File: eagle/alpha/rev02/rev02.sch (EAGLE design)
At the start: 379 parts, among them CN1 HOST, CN2 HOST, IC1 IS45S32160F, IC2 IS45S32160F, IC3 N25Q128A13ES, IC4 N25Q128A13ES, Q1 2N7002, Q3 2N7002, Q5 ASFL1, Q6 2N7002, T1 BC847, T2 BC847, T3 BC818, U1 MC14551BDG, U2 MC74HC1G14DTT1G, U3 ATTINY828R-AU, U4 MC14551BDG, U5 23K640-I/SN, U6 MCP79412-I/SN, U7 XC7A200TFBG484, Y1 12 MHz, Y2 12 MHz

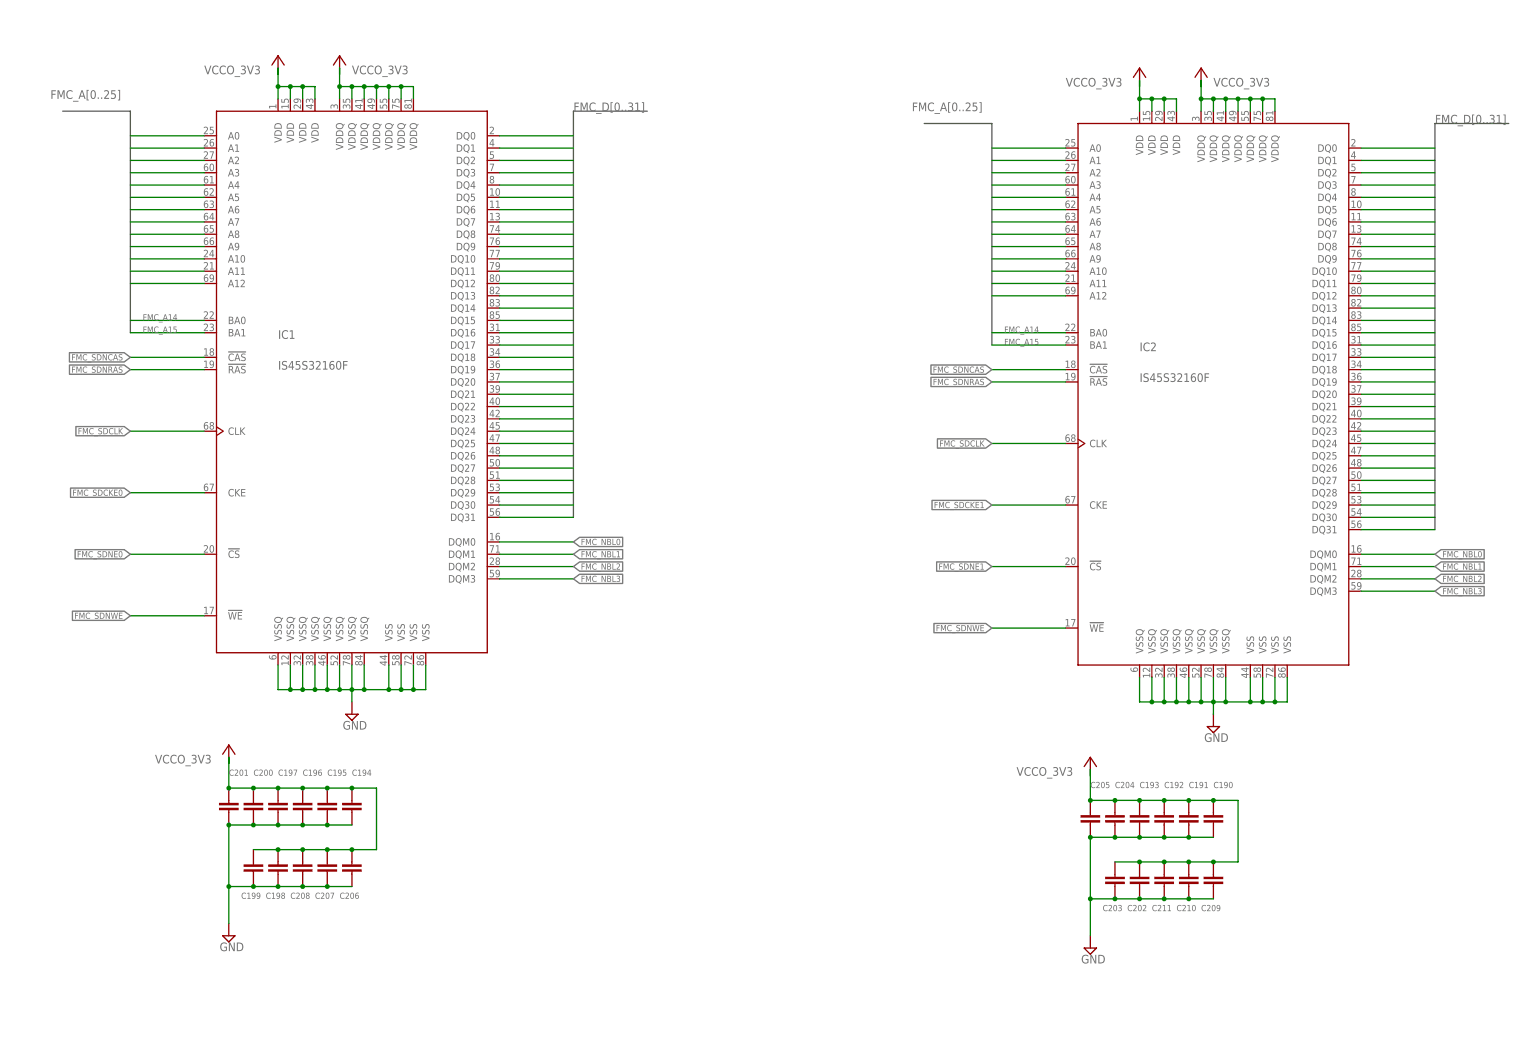
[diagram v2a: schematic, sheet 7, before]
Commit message: add SPI mux for FPGA cfg memory, and some other minor things.
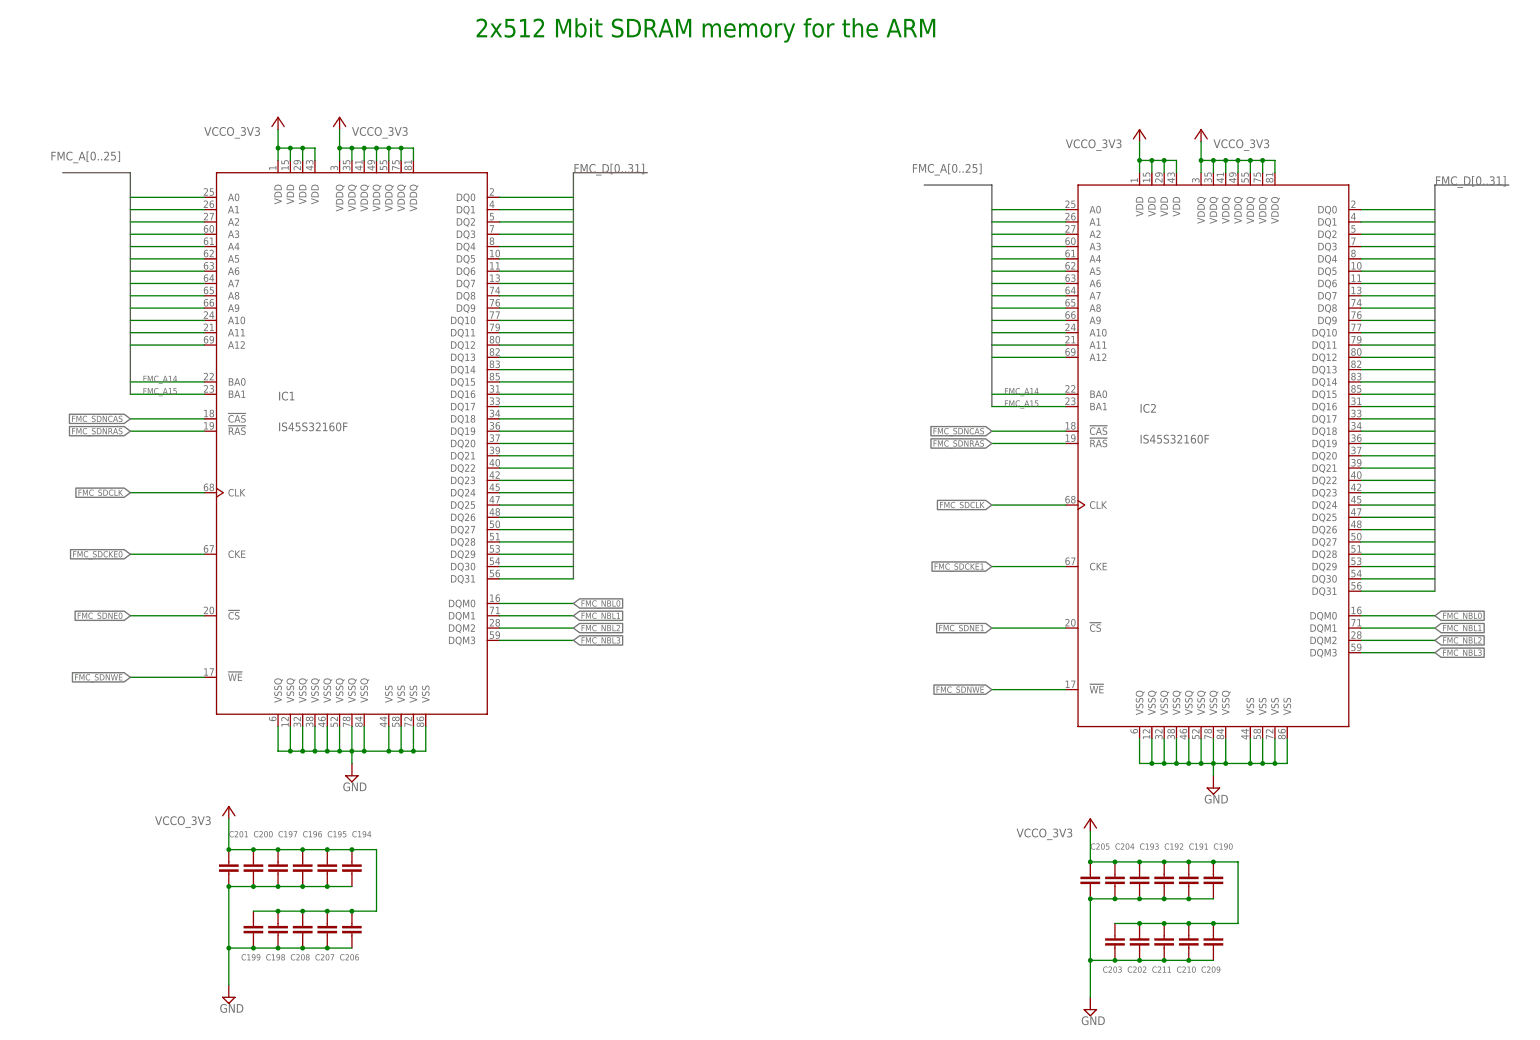
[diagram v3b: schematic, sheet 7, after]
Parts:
- removed C8: 0.1 uF, resistor:C-EUC0402
- removed R32: 15K, resistor:R-EU_R0603
- removed U1: MC14551BDG, ON_Semiconductor-MC14551BDG:MC14551BDG
- added C214: 0.1uF, resistor:C-EUC0402
- added IC5: 74AC244DW, 74xx-eu:74AC244DW
- added JP9: (no value), jumper:JP1Q
- added R77, R80, R81: 4.7k, resistor:R-EU_R0603
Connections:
- net ARM_FPGA_CFG_CONTROL renamed FPGA_CFG_CTRL_ARM_ENA
- removed net N$3: JP8.1, R32.2, U1.CONTROL
- new net FPGA_CFG_CTRL_FPGA_DIS: JP9.2, U$1IO.PJ5
- new net FPGA_PROM_CS_N: IC3.!S, IC5A.Y1, IC5B.Y1, R77.1, R9.1
- new net SPI_A_TRISTATE: IC5A.G, JP8.1, R80.1
- new net SPI_B_TRISTATE: IC5B.G, JP9.1, R81.1
- net 3V3_BATT: no longer C8.1, U1.VDD
- net ARM_FPGA_CFG_CS_N: now also IC5A.A1, U$1IO.PB12; no longer U1.X1
- net ARM_FPGA_CFG_MISO: now also IC5A.Y4; no longer U1.W1
- net ARM_FPGA_CFG_MOSI: now also IC5A.A3; no longer U1.Y1
- net ARM_FPGA_CFG_SCLK: now also IC5A.A2; no longer U1.Z1
- net ARM_LED1: now also U$1IO.PJ0; no longer U$1IO.PJ4
- net ARM_LED2: now also U$1IO.PJ1; no longer U$1IO.PJ3
- net ARM_LED4: now also U$1IO.PJ3; no longer U$1IO.PJ1
- net AVR_GPIO_11: now also U$1IO.PC14
- net FPGA_CFG_CS_N: now also IC5B.A1; no longer U1.X
- net FPGA_CFG_MISO: now also IC5B.Y4; no longer U1.W
- net FPGA_CFG_MOSI: now also IC5B.A3; no longer U1.Y
- net FPGA_CFG_SCLK: now also IC5B.A2; no longer U1.Z
- net FPGA_DONE: now also U$1IO.PJ15; no longer U$1IO.PJ7
- net FPGA_INIT_B: now also U$1IO.PJ7; no longer U$1IO.PJ14
- net FPGA_IRQ_N_0: now also U$1IO.PJ10; no longer U$1IO.PJ13
- net FPGA_IRQ_N_1: now also U$1IO.PJ11; no longer U$1IO.PJ12
- net FPGA_IRQ_N_2: now also U$1IO.PJ12; no longer U$1IO.PJ11
- net FPGA_IRQ_N_3: now also U$1IO.PJ13; no longer U$1IO.PJ10
- net FPGA_PROGRAM_B: now also U$1IO.PJ8; no longer U$1IO.PJ15
- net FPGA_PROM_MISO: now also IC5A.A4, IC5B.A4; no longer U1.W0
- net FPGA_PROM_MOSI: now also IC5A.Y3, IC5B.Y3; no longer U1.Y0
- net FPGA_PROM_SCLK: now also IC5A.Y2, IC5B.Y2; no longer U1.Z0
- net FT_CTS: now also U$1IO.USART2_RTS/PA1; no longer U$1IO.USART2_CTS/WKUP/PA0
- net FT_DTR: now also U$1IO.PA4
- net FT_MGMT_CTS: now also U$1IO.USART1_RTS/PA12; no longer U$1IO.USART1_CTS/PA11
- net FT_MGMT_DTR: now also U$1IO.PA8
- net FT_MGMT_RTS: now also U$1IO.USART1_CTS/PA11; no longer U$1IO.USART1_RTS/PA12
- net FT_MGMT_VPHY: now also C183.1, C184.1, FB4.P$2
- net FT_RTS: now also U$1IO.USART2_CTS/WKUP/PA0; no longer U$1IO.USART2_RTS/PA1
- net FT_VPHY: no longer C183.1, C184.1, FB4.P$2
- net GND: now also C214.2, IC5P.GND, R81.2; no longer C8.2, R32.1, U1.VEE, U1.VSS
- net KSM_PROM_CS_N: no longer IC3.!S, R9.1, U1.X0
- net RTC_MFP: now also U$1IO.PH3; no longer U$1IO.PH3/FMC_SDNE0
- net RTC_SDA: now also U$1IO.I2C2_SDA/PH5; no longer U$1IO.I2C2_SDA/FMC_SDNWE/PH5
- net SDIO_CK: now also U$1IO.SDIO_CK/PC12; no longer U$1IO.SDIO_CK/SPI3_MOSI/PC12
- net SDIO_D2: now also U$1IO.SDIO_D2/PC10; no longer U$1IO.SDIO_D2/SPI3_SCK/PC10
- net SDIO_D3: now also U$1IO.SDIO_D3/PC11; no longer U$1IO.SDIO_D3/SPI3_MISO/PC11
- net VCCO_3V3: now also C214.1, IC5P.VCC, R77.2, R80.2
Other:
- note added: "2x512 Mbit SDRAM memory for the ARM"
- note added: "ARM access default disabled through pull-up"
- note added: "All of these input/outputs can be swapped with equivalent functionality pins."
- note added: "Analog switch controlling access to the MKM. XXX suggest changing this chip to an 74AC244, like the one used for the FPGA config memory."
- note added: "Application access USB UART"
- note added: "Entropy source power"
- note added: "FPGA access default enabled through pull-down"
- note added: "FPGA config memory, 128 Mbit"
- note added: "Keystore memory, 128 Mbit"
- note added: "SPI mux to let ARM override access to FPGA config memory (to reprogram FPGA)"
- note added: "This memory holds cryptographic keys wrapped with the master key."
- note removed: "*) FPGA_GPIO_*, FPGA_IRQ_N_* and FPGA_{PROGRAM,INIT}_B signals can be swapped with any other available GPIO on the ARM"
- note removed: "Analog switch"
- note removed: "Analog switch to boot FPGA from config memory, or from ARM XXX this probably needs more HW support. FPGA is SPI master when booting from config memory, but should be SPI slave when being fed a bitstream from the ARM."
- note removed: "FPGA config memory"
- note removed: "FPGA_DONE can be swapped with any other available GPIO pin on the ARM"
- note removed: "Keystore memory This memory holds cryptographic keys wrapped with master key in MKM."
- note removed: "Pull-down CONTROL to enable 0 (PROM) by default"
- note removed: "XXX are jumpers on the ARM SPI nets really needed, when CONTROL defaults to the PROM?"
- note removed: "XXX check with Joachim if it is enough that STM32 can rewrite FPGA config memory"
- note removed: "XXX cross RTS/CTS?"
- note removed: "XXX test this circuit"
- moved on the sheet: C1, C110, C134, C190, C191, C192, C193, C194, C195, C196, C197, C198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

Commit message: add device prefixes and renumber all components
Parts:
- removed C214: 0.1uF, resistor:C-EUC0402
- removed IC4: N25Q128A13ES, altera-configdevices:N25Q128A13ES
- removed IC5: 74AC244DW, 74xx-eu:74AC244DW
- removed LED11: BLUE, led:LEDCHIP-LED0603
- removed LED12, LED16: GREEN, led:LEDCHIP-LED0603
- removed LED13: YELLOW, led:LEDCHIP-LED0603
- removed LED14, LED15: RED, led:LEDCHIP-LED0603
- removed LED7: YELLOW, SparkFun-LED:LED0603
- removed LED8: RED, SparkFun-LED:LED0603
- removed R80, R81: 4.7k, resistor:R-EU_R0603
- removed U$1: STM32F429BIT6, Alpha-IC:STM32F429BIT6
- removed U$10, U$3: FT232H_SERIAL, FT232H:FT232H_SERIAL
- removed U$2: STM32-SWD, STM32-SWD-connector:STM32-SWD
- removed U$9: LT3060ITS8-15, Alpha-Power:LT3060ITS8-15
- added C8: 47 uF, resistor:C-EUC1210
- added D10, D2: GREEN, SparkFun-LED:LED0603
- added D11: RED, SparkFun-LED:LED0603
- added D12: BLUE, SparkFun-LED:LED0603
- added D13: YELLOW, SparkFun-LED:LED0603
- added D14, D15, D16: BAT54, diode:BAT54
- added J1: STM32-SWD, STM32-SWD-connector:STM32-SWD
- added R32: 15K, resistor:R-EU_R0603
- added R78: 330, resistor:R-EU_R0603
- added U10: ATTINY828R-AU, ATMEL-ATTINY828R-AU:ATTINY828R-AU
- added U11: MC14551BDG, ON_Semiconductor-MC14551BDG:MC14551BDG
- added U12: 23K640-I/SN, Microchip-23K640-I_SN:23K640-I/SN
- added U13: XC7A200TFBG484, Xilinx_XC7A200TFBG484:XC7A200TFBG484
- added U8, U9: FT232H_SERIAL, Alpha-IC:FT232H_SERIAL
- C1: value 10NF -> 10 uF; device rcl:C-EUC0402 -> resistor:C-EUC1210; DIELECTRIC C0G -> X7R; RATED_VOLTAGE 25V -> 50V; TOLERANCE (none) -> 10%
- C10, C9: value 0.1 uF -> 330uF; device resistor:C-EUC0402 -> rc-master:CP_E-035X080; DIELECTRIC X7R -> (none); TOLERANCE (none) -> 20%
- C100, C101, C105, C106, C107, C73, C74, C76, C79, C81, C83, C84, C85, C88, C89, C98: value 0.47 uF -> 0.1 uF; DIELECTRIC X5R -> X7R; RATED_VOLTAGE 6.3V -> 10V; TOLERANCE 10% -> (none)
- C102, C77, C80, C92: value 0.47 uF -> 10 uF; device resistor:C-EUC0402 -> resistor:C-EUC0805; DIELECTRIC X5R -> X7R; RATED_VOLTAGE 6.3V -> 10V; TOLERANCE 10% -> (none)
- C103: value 0.47uF -> 0.1 uF; device resistor:C-EUC0603 -> resistor:C-EUC0402; DIELECTRIC X5R -> X7R; RATED_VOLTAGE 16V -> 10V; TOLERANCE 10% -> (none)
- C104: value 10 uF -> 0.1 uF; device resistor:C-EUC1210 -> resistor:C-EUC0402; RATED_VOLTAGE 50V -> 10V; TOLERANCE 10% -> (none)
- C108, C109, C121, C122: value 0.47 uF -> 0.1 uF; device resistor:C-EUC0402 -> resistor:C-EUC0603; DIELECTRIC X5R -> X7R; RATED_VOLTAGE 6.3V -> 50V
- C11, C12: value 5 pF -> 10NF; device rcl:C-EUC0603 -> rcl:C-EUC0402; RATED_VOLTAGE 10V -> 25V
- C110: value 0.01 uF -> 0.1uF; device resistor:C-EUC0603 -> resistor:C-EUC0402; DIELECTRIC X7R -> (none); RATED_VOLTAGE 50V -> (none); TOLERANCE 10% -> (none)
- C111: value 330uF -> 0.01 uF; device rc-master:CP_E-035X080 -> resistor:C-EUC0603; DIELECTRIC (none) -> X7R; RATED_VOLTAGE 10V -> 50V; TOLERANCE 20% -> 10%
- C112: value 330uF -> 0.1 uF; device rc-master:CP_E-035X080 -> resistor:C-EUC0603; DIELECTRIC (none) -> X7R; RATED_VOLTAGE 10V -> 50V; TOLERANCE 20% -> 10%
- C113: value 0.47 uF -> 22 uF; device resistor:C-EUC0402 -> resistor:C-EUC1210; RATED_VOLTAGE 6.3V -> 16V; TOLERANCE 10% -> 20%
- C114: value 0.047uF -> 22 uF; device resistor:C-EUC0603 -> resistor:C-EUC1210; DIELECTRIC X7R -> X5R; RATED_VOLTAGE 50V -> 16V; TOLERANCE 10% -> 20%
- C117, C118: value 0.47 uF -> 27pF; device resistor:C-EUC0402 -> resistor:C-EUC0603; DIELECTRIC X5R -> C0G; RATED_VOLTAGE 6.3V -> 50V; TOLERANCE 10% -> 5%
- C119, C120, C126: value 0.47 uF -> 47 uF; device resistor:C-EUC0402 -> resistor:C-EUC1210; RATED_VOLTAGE 6.3V -> 16V; TOLERANCE 10% -> 20%
- C123, C127: value 0.47 uF -> 330 uF; device resistor:C-EUC0402 -> resistor:CPOL-EUSMCD; DIELECTRIC X5R -> TANTALUM
- C13: value 0.1 uF -> 2.2 uF LowESR; device rcl:C-EUC0603 -> resistor:C-EUC0603; DIELECTRIC (none) -> X7R; RATED_VOLTAGE (none) -> 25V
- C131: value 27pF -> 0.47 uF; device resistor:C-EUC0603 -> resistor:C-EUC0402; DIELECTRIC C0G -> X5R; RATED_VOLTAGE 50V -> 6.3V; TOLERANCE 5% -> 10%
- C132: value 27pF -> 4.7 uF; DIELECTRIC C0G -> X5R; RATED_VOLTAGE 50V -> 16V; TOLERANCE 5% -> 10%
- C133, C137: value 0.1 uF -> 47 uF; device resistor:C-EUC0603 -> resistor:C-EUC1210; DIELECTRIC X7R -> X5R; RATED_VOLTAGE 50V -> 16V; TOLERANCE 10% -> 20%
- C134, C135, C138: value 0.1 uF -> 0.47 uF; device resistor:C-EUC0603 -> resistor:C-EUC0402; DIELECTRIC X7R -> X5R; RATED_VOLTAGE 50V -> 6.3V
- C136, C139: value 0.1 uF -> 4.7 uF; DIELECTRIC X7R -> X5R; RATED_VOLTAGE 50V -> 16V
- C14, C15: value 5 pF -> 0.1 uF; device rcl:C-EUC0402 -> rcl:C-EUC0603; DIELECTRIC C0G -> (none)
- C140, C141: value 10 uF -> 4.7 uF; device resistor:C-EUC1210 -> resistor:C-EUC0603; DIELECTRIC X7R -> X5R; RATED_VOLTAGE 50V -> 16V
- C142, C143, C146, C147, C150, C151, C154, C155, C158, C159, C162, C163, C164: value 4.7 uF -> 0.47 uF; device resistor:C-EUC0603 -> resistor:C-EUC0402; RATED_VOLTAGE 16V -> 6.3V
- C16: value 10 uF -> 0.1 uF; device resistor:C-EUC0805 -> rcl:C-EUC0603; DIELECTRIC X7R -> (none); RATED_VOLTAGE 10V -> (none)
- C165, C166, C167: value 4.7 uF -> 47 uF; device resistor:C-EUC0603 -> resistor:C-EUC1210; TOLERANCE 10% -> 20%
- C169, C170, C171, C172, C173, C174, C175, C176, C177, C178: value 47 uF -> 4.7 uF; device resistor:C-EUC1210 -> resistor:C-EUC0603; TOLERANCE 20% -> 10%
- C17: value 10 uF -> 5 pF; device resistor:C-EUC0805 -> rcl:C-EUC0402; DIELECTRIC X7R -> C0G; RATED_VOLTAGE 10V -> (none)
- C179: DIELECTRIC X7R -> X5R; RATED_VOLTAGE 10V -> 16V; TOLERANCE (none) -> 10%
- C18: value 0.1uF -> 5 pF; device resistor:C-EUC0402 -> rcl:C-EUC0402; DIELECTRIC X7R -> C0G; RATED_VOLTAGE 10V -> (none)
- C180: value 0.1 uF -> 4.7 uF; device resistor:C-EUC0402 -> resistor:C-EUC0603; DIELECTRIC X7R -> X5R; RATED_VOLTAGE 10V -> 16V; TOLERANCE (none) -> 10%
- C181: value 4.7 uF -> 0.47 uF; device resistor:C-EUC0603 -> resistor:C-EUC0402; DIELECTRIC X7R -> X5R; RATED_VOLTAGE 10V -> 6.3V; TOLERANCE (none) -> 10%
- C182, C183, C185, C187, C188, C189, C193, C197, C200, C201, C204: value 0.1 uF -> 0.47 uF; DIELECTRIC X7R -> X5R; RATED_VOLTAGE 10V -> 6.3V; TOLERANCE (none) -> 10%
- C184, C186: value 10 uF -> 0.47 uF; device resistor:C-EUC0805 -> resistor:C-EUC0402; DIELECTRIC X7R -> X5R; RATED_VOLTAGE 10V -> 6.3V; TOLERANCE (none) -> 10%
- C190, C191, C192, C194, C195, C196, C198, C199, C202, C203: value 0.1uF -> 0.47 uF; DIELECTRIC X7R -> X5R; RATED_VOLTAGE 10V -> 6.3V; TOLERANCE (none) -> 10%
- C2, C3: value 0.1 uF -> 10 uF; device rcl:C-EUC0603 -> resistor:C-EUC1210; DIELECTRIC (none) -> X7R; RATED_VOLTAGE (none) -> 50V; TOLERANCE (none) -> 10%
- C205: value 0.1 uF -> 22 uF; device resistor:C-EUC0402 -> resistor:C-EUC1210; DIELECTRIC X7R -> X5R; RATED_VOLTAGE 10V -> 16V; TOLERANCE (none) -> 20%
- C206: value 0.1uF -> 22 uF; device resistor:C-EUC0402 -> resistor:C-EUC1210; DIELECTRIC X7R -> X5R; RATED_VOLTAGE 10V -> 16V; TOLERANCE (none) -> 20%
- C207, C6: value 0.1uF -> 0.047uF; device resistor:C-EUC0402 -> resistor:C-EUC0603; RATED_VOLTAGE 10V -> 50V; TOLERANCE (none) -> 10%
- C208: value 0.1uF -> 27pF; device resistor:C-EUC0402 -> resistor:C-EUC0603; DIELECTRIC X7R -> C0G; RATED_VOLTAGE 10V -> 50V; TOLERANCE (none) -> 5%
- C209, C210: value 0.1uF -> 47 uF; device resistor:C-EUC0402 -> resistor:C-EUC1210; DIELECTRIC X7R -> X5R; RATED_VOLTAGE 10V -> 16V; TOLERANCE (none) -> 20%
- C21: value 0.1uF -> 1 uF; device resistor:C-EUC0402 -> resistor:C-EUC0603
- C211: value 0.1uF -> 0.1 uF; device resistor:C-EUC0402 -> resistor:C-EUC0603; RATED_VOLTAGE 10V -> 50V; TOLERANCE (none) -> 10%
- C213: value 2.2 uF LowESR -> 0.1 uF; RATED_VOLTAGE 25V -> 50V; TOLERANCE (none) -> 10%
- C22, C23, C24: value 0.1uF -> 2.2 uF; device resistor:C-EUC0402 -> resistor:C-EUC0603
- C25: value 0.1 uF -> 2.2 uF; device resistor:C-EUC0402 -> resistor:C-EUC0603
- C26, C27: value 0.1uF -> 10 uF; device resistor:C-EUC0402 -> resistor:C-EUC0805
- C30: value 1 uF -> 0.1uF; device resistor:C-EUC0603 -> resistor:C-EUC0402
- C31: value 0.1uF -> 0.1 uF
- C38, C39, C56, C57: value 2.2 uF -> 0.1uF; device resistor:C-EUC0603 -> resistor:C-EUC0402
- C4: value 10NF -> 0.047uF; device rcl:C-EUC0402 -> resistor:C-EUC0603; DIELECTRIC C0G -> X7R; RATED_VOLTAGE 25V -> 50V; TOLERANCE (none) -> 10%
- C41, C42, C46, C49, C51, C53, C54, C55, C60, C62: value 0.1 uF -> 0.1uF
- C43, C44: value 5 pF -> 0.1uF; device rcl:C-EUC0603 -> resistor:C-EUC0402; DIELECTRIC C0G -> X7R
- C45: value 4.7 uF -> 0.1uF; device resistor:C-EUC0603 -> resistor:C-EUC0402
- C47: value 4.7 uF -> 0.1 uF; device resistor:C-EUC0603 -> resistor:C-EUC0402
- C5: value 2.2 uF LowESR -> 0.47uF; DIELECTRIC X7R -> X5R; RATED_VOLTAGE 25V -> 16V; TOLERANCE (none) -> 10%
- C50, C58: value 10 uF -> 0.1 uF; device resistor:C-EUC0805 -> resistor:C-EUC0402
- C52: value 10 uF -> 0.1uF; device resistor:C-EUC0805 -> resistor:C-EUC0402
- C63, C64: value 5pF -> 0.1uF; device rcl:C-EUC0603 -> resistor:C-EUC0402; DIELECTRIC (none) -> X7R; RATED_VOLTAGE (none) -> 10V
- C65: value 330 uF -> 0.1uF; device resistor:CPOL-EUSMCD -> resistor:C-EUC0402; DIELECTRIC TANTALUM -> X7R; RATED_VOLTAGE 6.3V -> 10V; TOLERANCE 10% -> (none)
- C66: value 4.7 uF -> 0.1uF; device resistor:C-EUC0603 -> resistor:C-EUC0402; DIELECTRIC X5R -> X7R; RATED_VOLTAGE 16V -> 10V; TOLERANCE 10% -> (none)
- C67: value 0.47 uF -> 0.1uF; DIELECTRIC X5R -> X7R; RATED_VOLTAGE 6.3V -> 10V; TOLERANCE 10% -> (none)
- C68: value 47 uF -> 0.1uF; device resistor:C-EUC1210 -> resistor:C-EUC0402; DIELECTRIC X5R -> X7R; RATED_VOLTAGE 16V -> 10V; TOLERANCE 20% -> (none)
- C69: value 330 uF -> 0.1 uF; device resistor:CPOL-EUSMCD -> resistor:C-EUC0603; DIELECTRIC TANTALUM -> X7R; RATED_VOLTAGE 6.3V -> 50V
- C7: value 0.1 uF -> 2.2 uF LowESR; device resistor:C-EUC0402 -> resistor:C-EUC0603; RATED_VOLTAGE 10V -> 25V
- C70: value 0.1 uF -> 5pF; device resistor:C-EUC0603 -> rcl:C-EUC0603; DIELECTRIC X7R -> (none); RATED_VOLTAGE 50V -> (none); TOLERANCE 10% -> (none)
- C71: value 0.47 uF -> 5pF; device resistor:C-EUC0402 -> rcl:C-EUC0603; DIELECTRIC X5R -> (none); RATED_VOLTAGE 6.3V -> (none); TOLERANCE 10% -> (none)
- C72, C82, C97: value 0.47 uF -> 4.7 uF; device resistor:C-EUC0402 -> resistor:C-EUC0603; DIELECTRIC X5R -> X7R; RATED_VOLTAGE 6.3V -> 10V; TOLERANCE 10% -> (none)
- C75, C78, C90, C93: value 0.47 uF -> 5 pF; device resistor:C-EUC0402 -> rcl:C-EUC0603; DIELECTRIC X5R -> C0G; RATED_VOLTAGE 6.3V -> 10V; TOLERANCE 10% -> (none)
- C86, C94: value 0.047uF -> 0.1 uF; device resistor:C-EUC0603 -> resistor:C-EUC0402; RATED_VOLTAGE 50V -> 10V; TOLERANCE 10% -> (none)
- C87: value 22 uF -> 4.7 uF; device resistor:C-EUC1210 -> resistor:C-EUC0603; DIELECTRIC X5R -> X7R; RATED_VOLTAGE 16V -> 10V; TOLERANCE 20% -> (none)
- C91, C96: value 22 uF -> 0.1 uF; device resistor:C-EUC1210 -> resistor:C-EUC0402; DIELECTRIC X5R -> X7R; RATED_VOLTAGE 16V -> 10V; TOLERANCE 20% -> (none)
- C95: value 22 uF -> 10 uF; device resistor:C-EUC1210 -> resistor:C-EUC0805; DIELECTRIC X5R -> X7R; RATED_VOLTAGE 16V -> 10V; TOLERANCE 20% -> (none)
- C99: value 27pF -> 0.1 uF; device resistor:C-EUC0603 -> resistor:C-EUC0402; DIELECTRIC C0G -> X7R; RATED_VOLTAGE 50V -> 10V; TOLERANCE 5% -> (none)
- D3: value BAT54 -> RED; device diode:BAT54 -> SparkFun-LED:LED0603
- D4: value BAT54 -> BLUE; device diode:BAT54 -> SparkFun-LED:LED0603
- D5: value BAT54 -> YELLOW; device diode:BAT54 -> SparkFun-LED:LED0603
- IC1: value IS45S32160F -> N25Q128A13ES; device Alpha-IC:IS45S32160F -> altera-configdevices:N25Q128A13ES
- IC2: value IS45S32160F -> 74AC244DW; device Alpha-IC:IS45S32160F -> 74xx-eu:74AC244DW
- JP4: device jumper:JP1Q -> SparkFun-Connectors:M03LOCK
- JP6: device SparkFun-Connectors:M03LOCK -> jumper:JP1Q
- LED1: value BLUE -> RED; device SparkFun-LED:LED0603 -> led:LEDCHIP-LED0603
- LED2: value GREEN -> RED; device SparkFun-LED:LED0603 -> led:LEDCHIP-LED0603
- LED3: value YELLOW -> GREEN; device SparkFun-LED:LED0603 -> led:LEDCHIP-LED0603
- LED4: value RED -> YELLOW; device SparkFun-LED:LED0603 -> led:LEDCHIP-LED0603
- LED5, LED6: device SparkFun-LED:LED0603 -> led:LEDCHIP-LED0603
- Q3: value 2N7002 -> (none); device transistors_gaui:2N7002 -> adafruit:XTAL-4-3225; MPN (none) -> ABM8G-25.000MHZ-4Y-T3; OC_FARNELL (none) -> 2467848
- Q4: value (none) -> 2N7002; device adafruit:XTAL-4-3225 -> transistors_gaui:2N7002; MPN ABM8G-25.000MHZ-4Y-T3 -> (none); OC_FARNELL 2467848 -> (none)
- R1: value 1K -> 56k; TOLERANCE (none) -> 1%
- R10: value 10K -> 470; device resistor:R-EU_R0402 -> resistor:R-EU_R0603
- R11: value 10K -> 1K; device resistor:R-EU_R0402 -> resistor:R-EU_R0603
- R12: value 0 -> 10K; device resistor:R-EU_R0402 -> resistor:R-EU_R0603
- R13: value 12K -> 1K; device resistor:R-EU_R0402 -> resistor:R-EU_R0603; TOLERANCE 1% -> (none)
- R14: value 220 -> 0
- R15: value 220 -> 10K
- R16: value 15K -> 330R; device resistor:R-EU_R0402 -> Panasonic-EXB-ERJ:EXB38V331JV
- R17, R18: value 15K -> 4.7k; TOLERANCE (none) -> 5%
- R19: value 15K -> 10K; device resistor:R-EU_R0603 -> resistor:R-EU_R0402
- R2: value 1K -> 4.64k; TOLERANCE (none) -> 1%
- R20: value 4.7k -> 10K; device resistor:R-EU_R0603 -> resistor:R-EU_R0402; TOLERANCE 5% -> (none)
- R21, R23, R27: value 1.0k -> 10K; device resistor:R-EU_R0603 -> resistor:R-EU_R0402; TOLERANCE 5% -> (none)
- R22: value 10K -> 12K; TOLERANCE (none) -> 1%
- R24: value 1.0k -> 220; device resistor:R-EU_R0603 -> resistor:R-EU_R0402; TOLERANCE 5% -> (none)
- R25, R29: value 4.7k -> 220; device resistor:R-EU_R0603 -> resistor:R-EU_R0402; TOLERANCE 5% -> (none)
- R26: value 4.7k -> 12K; device resistor:R-EU_R0603 -> resistor:R-EU_R0402; TOLERANCE 5% -> 1%
- R28: value 0 -> 220; device resistor:R-EU_R0603 -> resistor:R-EU_R0402
- R3: value 330R -> 100; device Panasonic-EXB-ERJ:EXB38V331JV -> resistor:R-EU_R0603; TOLERANCE (none) -> 5%
- R30: value 10K -> 15K
- R31: value 10K -> 330R; device resistor:R-EU_R0402 -> Panasonic-EXB-ERJ:EXB38V331JV
- R33: value 330 -> 15K; TOLERANCE 5% -> (none)
- R34: value 100 -> 15K; TOLERANCE 5% -> (none)
- R35, R36, R37: value 10k -> 1.0k
- R38: value 62k -> 330
- R39: value 4.7k -> 100
- R4: value 10K -> 0
- R40: value 205k -> 4.7k; TOLERANCE 1% -> 5%
- R41: value 147k -> 4.7k; TOLERANCE 1% -> 5%
- R42: value 470 -> 4.7k
- R43: value 0 -> 10k; device resistor:R-EU_R1206 -> resistor:R-EU_R0603; TOLERANCE (none) -> 5%
- R44: value 62k -> 10k
- R45: value 4.7k -> 10k
- R46: value 205k -> 4.7k; TOLERANCE 1% -> (none)
- R47: value 59k -> 4.7k; TOLERANCE 1% -> (none)
- R48: value 470 -> 4.7k; TOLERANCE 5% -> (none)
- R49: device resistor:R-EU_R1206 -> resistor:R-EU_R0603
- R5: value 470 -> 1K; device resistor:R-EU_R0603 -> resistor:R-EU_R0402; TOLERANCE (none) -> 5%
- R51: value 150k -> 4.7k; TOLERANCE 1% -> 5%
- R52: value 226k -> 4.7k; TOLERANCE 1% -> 5%
- R53: value 0 -> 62k; device resistor:R-EU_R1206 -> resistor:R-EU_R0603; TOLERANCE (none) -> 5%
- R54: value 100 -> 4.7k
- R55: value 100k -> 62k; TOLERANCE 1% -> 5%
- R56, R58: value 4.7k -> 205k; TOLERANCE 5% -> 1%
- R57: value 100k -> 147k
- R59: value 100k -> 59k
- R6, R77: TOLERANCE (none) -> 5%
- R60: value 4.7k -> 470
- R61: value 330 -> 470
- R62: value 100 -> 0; device resistor:R-EU_R0603 -> resistor:R-EU_R1206; TOLERANCE 5% -> (none)
- R63: value 4.64k -> 0; device resistor:R-EU_R0603 -> resistor:R-EU_R1206; TOLERANCE 1% -> (none)
- R64: value 56k -> 330R; device resistor:R-EU_R0603 -> Panasonic-EXB-ERJ:EXB38V331JV; TOLERANCE 1% -> (none)
- R65: value 6.3k -> 1.0k; TOLERANCE 1% -> 5%
- R66: value 1.21k -> 4.7k; TOLERANCE 1% -> 5%
- R68: value 0 -> 150k; TOLERANCE (none) -> 1%
- R69: value 10K -> 226k; device resistor:R-EU_R0402 -> resistor:R-EU_R0603; TOLERANCE (none) -> 1%
- R7: value 330R -> 10K; device Panasonic-EXB-ERJ:EXB38V331JV -> resistor:R-EU_R0402
- R70: value 12K -> 100; device resistor:R-EU_R0402 -> resistor:R-EU_R0603; TOLERANCE 1% -> 5%
- R71: value 220 -> 0; device resistor:R-EU_R0402 -> resistor:R-EU_R1206
- R72: value 220 -> 100k; device resistor:R-EU_R0402 -> resistor:R-EU_R0603; TOLERANCE (none) -> 1%
- R74: value 4.7k -> 100k; TOLERANCE 5% -> 1%
- R75: value 10K -> 4.7k; device resistor:R-EU_R0402 -> resistor:R-EU_R0603
- R76: value 1K -> 100k; device resistor:R-EU_R0402 -> resistor:R-EU_R0603; TOLERANCE 5% -> 1%
- R8: value 330R -> 6.3k; device Panasonic-EXB-ERJ:EXB38V331JV -> resistor:R-EU_R0603; TOLERANCE (none) -> 1%
- R9: value 4.7k -> 1.21k; TOLERANCE 5% -> 1%
- SV1: device con-lstb:MA08-2 -> con-lstb:MA08-1
- SV3: device con-lstb:MA08-1 -> con-lstb:MA08-2
- U2: value MC74HC1G14DTT1G -> LT3060ITS8-15; device MC74HC1G14DTT1G:MC74HC1G14DTT1G -> Alpha-Power:LT3060ITS8-15
- U3: value ATTINY828R-AU -> MC74HC1G14DTT1G; device ATMEL-ATTINY828R-AU:ATTINY828R-AU -> MC74HC1G14DTT1G:MC74HC1G14DTT1G
- U4: value MC14551BDG -> STM32F429BIT6; device ON_Semiconductor-MC14551BDG:MC14551BDG -> Alpha-IC:STM32F429BIT6
- U5: value 23K640-I/SN -> IS45S32160F; device Microchip-23K640-I_SN:23K640-I/SN -> Alpha-IC:IS45S32160F
- U6: value MCP79412-I/SN -> IS45S32160F; device MCP79412:MCP79412-I/SN -> Alpha-IC:IS45S32160F
- U7: value XC7A200TFBG484 -> MCP79412-I/SN; device Xilinx_XC7A200TFBG484:XC7A200TFBG484 -> MCP79412:MCP79412-I/SN
- renumbered LED10 to D7, LED17 to D8, LED18 to D9, LED9 to D6, T3 to Q2, U$4 to S2, U$5 to U14, U$6 to U15, U$7 to U16, U$8 to U1
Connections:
- net 15V_LDO_ENABLE: now also R7.2, U2.!SHDN; no longer R22.2, U$9.!SHDN
- net 15V_STABLE: now also C11.2, C13.1, R11.1, U2.OUT; no longer C1.2, C5.1, R2.1, U$9.OUT
- net 3V3_BATT: now also C102.1, C103.1, C104.1, C106.1, C107.1, JP4.2, R30.2, R33.1, R34.2, U10.AVCC, U10.VCC, U11.VDD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; no longer C58.1, C59.1, C60.1, C61.1, C62.1, JP6.2, R16.2, R17.1, R18.2, U3.AVCC, U3.VCC, U4.VDD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
- net AGND: now also C16.1, T2.E, U3.GND; no longer C13.1, T1.E, U2.GND
- net AMPLIFIED: now also R12.2, R13.1, T2.C, TP2.TP, U3.IN_A; no longer R1.1, R4.2, T1.C, TP1.TP, U2.IN_A
- net AMP_P1: now also C15.2, R12.1, T2.B; no longer C2.2, R4.1, T1.B
- net ARM_FPGA_CFG_CS_N: now also IC2A.A1, U4IO.PB12; no longer IC5A.A1, U$1IO.PB12
- net ARM_FPGA_CFG_MISO: now also IC2A.Y4, U4IO.SPI2_MISO/PB14; no longer IC5A.Y4, U$1IO.SPI2_MISO/PB14
- net ARM_FPGA_CFG_MOSI: now also IC2A.A3, U4IO.SPI2_MOSI/PB15; no longer IC5A.A3, U$1IO.SPI2_MOSI/PB15
- net ARM_FPGA_CFG_SCLK: now also IC2A.A2, U4IO.SPI2_SCK/PB13; no longer IC5A.A2, U$1IO.SPI2_SCK/PB13
- net ARM_LED1: now also R16.5, U4IO.PJ0; no longer R8.5, U$1IO.PJ0
- net ARM_LED2: now also R16.6, U4IO.PJ1; no longer R8.6, U$1IO.PJ1
- net ARM_LED3: now also R16.7, U4IO.PJ2; no longer R8.7, U$1IO.PJ2
- net ARM_LED4: now also R16.8, U4IO.PJ3; no longer R8.8, U$1IO.PJ3
- net AVR_GPIO_1: now also U10.(PCINT18/ADC18/TOCC2/RXD/INT1)_PC2; no longer U3.(PCINT18/ADC18/TOCC2/RXD/INT1)_PC2
- net AVR_GPIO_10: now also U10.PB2_(PCINT10/ADC10), U4IO.PC13; no longer U$1IO.PC13, U3.PB2_(PCINT10/ADC10)
- net AVR_GPIO_11: now also U10.PB3_(PCINT11/ADC11), U4IO.PC14; no longer U$1IO.PC14, U3.PB3_(PCINT11/ADC11)
- net AVR_GPIO_2: now also U10.(PCINT19/ADC19/TOCC3/TXD)_PC3; no longer U3.(PCINT19/ADC19/TOCC3/TXD)_PC3
- net AVR_GPIO_3: now also U10.(PCINT20/ADC20/TOCC4)_PC4; no longer U3.(PCINT20/ADC20/TOCC4)_PC4
- net AVR_GPIO_4: now also U10.(PCINT21/ADC21/TOCC5/ICP1/T0)_PC5; no longer U3.(PCINT21/ADC21/TOCC5/ICP1/T0)_PC5
- net AVR_GPIO_5: now also U10.(PCINT22/ADC22/CLKI/TOCC6)_PC6; no longer U3.(PCINT22/ADC22/CLKI/TOCC6)_PC6
- net AVR_GPIO_6: now also U10.(PCINT23/ADC23/TOCC7/T1)_PC7; no longer U3.(PCINT23/ADC23/TOCC7/T1)_PC7
- net AVR_GPIO_7: now also U10.(PCINT0/ADC0)_PA0; no longer U3.(PCINT0/ADC0)_PA0
- net AVR_GPIO_8: now also U10.(PCINT1/ADC1/AIN0)_PA1; no longer U3.(PCINT1/ADC1/AIN0)_PA1
- net AVR_LED1: now also R31.5, U10.(PCINT7/ADC7)_PA7; no longer R7.5, U3.(PCINT7/ADC7)_PA7
- net AVR_LED2: now also R31.6, U10.(PCINT6/ADC6)_PA6; no longer R7.6, U3.(PCINT6/ADC6)_PA6
- net AVR_LED3: now also R31.7, U10.(PC!INT5/ADC5)_PA5; no longer R7.7, U3.(PC!INT5/ADC5)_PA5
- net AVR_LED4: now also R31.8, U10.(PCINT4/ADC4)_PA4; no longer R7.8, U3.(PCINT4/ADC4)_PA4
- net AVR_PANIC: now also U10.(PCINT2/ADC2/AIN1)_PA2; no longer U3.(PCINT2/ADC2/AIN1)_PA2
- net AVR_RESET: now also R30.1, U10.PD2_(!PCINT26/ADC26/RESET/DW); no longer R16.1, U3.PD2_(!PCINT26/ADC26/RESET/DW)
- net BOOT0: now also R15.2, U4CFG.BOOT0@197; no longer R10.2, U$1CFG.BOOT0@197
- net DIGITIZED_NOISE: now also U13B14.IO_L12P_T1_MRCC_14, U3.OUT_Y; no longer U2.OUT_Y, U7B14.IO_L12P_T1_MRCC_14
- net FMC_A0: now also U13B13.IO_0_13, U4FMC.FMC_A0/PF0, U5.A0, U6.A0; no longer IC1.A0, IC2.A0, U$1FMC.FMC_A0/PF0, U7B13.IO_0_13
- net FMC_A1: now also U13B13.IO_L1P_T0_13, U4FMC.FMC_A1/PF1, U5.A1, U6.A1; no longer IC1.A1, IC2.A1, U$1FMC.FMC_A1/PF1, U7B13.IO_L1P_T0_13
- net FMC_A10: now also U13B13.IO_L5N_T0_13, U4FMC.FMC_A10/PG0, U5.A10, U6.A10; no longer IC1.A10, IC2.A10, U$1FMC.FMC_A10/PG0, U7B13.IO_L5N_T0_13
- net FMC_A11: now also U13B13.IO_L6P_T0_13, U4FMC.FMC_A11/PG1, U5.A11, U6.A11; no longer IC1.A11, IC2.A11, U$1FMC.FMC_A11/PG1, U7B13.IO_L6P_T0_13
- net FMC_A12: now also U13B13.IO_L6N_T0_VREF_13, U4FMC.FMC_A12/PG2, U5.A12, U6.A12; no longer IC1.A12, IC2.A12, U$1FMC.FMC_A12/PG2, U7B13.IO_L6N_T0_VREF_13
- net FMC_A13: now also U13B13.IO_L7P_T1_13, U4FMC.FMC_A13/PG3; no longer U$1FMC.FMC_A13/PG3, U7B13.IO_L7P_T1_13
- net FMC_A14: now also U13B13.IO_L7N_T1_13, U4FMC.FMC_A14/PG4, U5.BA0, U6.BA0; no longer IC1.BA0, IC2.BA0, U$1FMC.FMC_A14/PG4, U7B13.IO_L7N_T1_13
- net FMC_A15: now also U13B13.IO_L8P_T1_13, U4FMC.FMC_A15/PG5, U5.BA1, U6.BA1; no longer IC1.BA1, IC2.BA1, U$1FMC.FMC_A15/PG5, U7B13.IO_L8P_T1_13
- net FMC_A16: now also U13B13.IO_L8N_T1_13, U4FMC.FMC_A16/PD11; no longer U$1FMC.FMC_A16/PD11, U7B13.IO_L8N_T1_13
- net FMC_A17: now also U13B13.IO_L9P_T1_DQS_13, U4FMC.FMC_A17/PD12; no longer U$1FMC.FMC_A17/PD12, U7B13.IO_L9P_T1_DQS_13
- net FMC_A18: now also U13B13.IO_L9N_T1_DQS_13, U4FMC.FMC_A18/PD13; no longer U$1FMC.FMC_A18/PD13, U7B13.IO_L9N_T1_DQS_13
- net FMC_A19: now also U13B13.IO_L10P_T1_13, U4FMC.FMC_A19/PE3; no longer U$1FMC.FMC_A19/PE3, U7B13.IO_L10P_T1_13
- net FMC_A2: now also U13B13.IO_L1N_T0_13, U4FMC.FMC_A2/PF2, U5.A2, U6.A2; no longer IC1.A2, IC2.A2, U$1FMC.FMC_A2/PF2, U7B13.IO_L1N_T0_13
- net FMC_A20: now also U13B13.IO_L10N_T1_13, U4FMC.FMC_A20/PE4; no longer U$1FMC.FMC_A20/PE4, U7B13.IO_L10N_T1_13
- net FMC_A21: now also U13B13.IO_L11P_T1_SRCC_13, U4FMC.FMC_A21/PE5; no longer U$1FMC.FMC_A21/PE5, U7B13.IO_L11P_T1_SRCC_13
- net FMC_A22: now also U13B13.IO_L11N_T1_SRCC_13, U4FMC.FMC_A22/PE6; no longer U$1FMC.FMC_A22/PE6, U7B13.IO_L11N_T1_SRCC_13
- net FMC_A23: now also U13B13.IO_L12N_T1_MRCC_13, U4FMC.FMC_A23/PE2; no longer U$1FMC.FMC_A23/PE2, U7B13.IO_L12N_T1_MRCC_13
- net FMC_A24: now also U13B13.IO_L13P_T2_MRCC_13, U4FMC.FMC_A24/PG13; no longer U$1FMC.FMC_A24/PG13, U7B13.IO_L13P_T2_MRCC_13
- net FMC_A25: now also U13B13.IO_L13N_T2_MRCC_13, U4FMC.FMC_A25/PG14; no longer U$1FMC.FMC_A25/PG14, U7B13.IO_L13N_T2_MRCC_13
- net FMC_A3: now also U13B13.IO_L2P_T0_13, U4FMC.FMC_A3/PF3, U5.A3, U6.A3; no longer IC1.A3, IC2.A3, U$1FMC.FMC_A3/PF3, U7B13.IO_L2P_T0_13
- net FMC_A4: now also U13B13.IO_L2N_T0_13, U4FMC.FMC_A4/PF4, U5.A4, U6.A4; no longer IC1.A4, IC2.A4, U$1FMC.FMC_A4/PF4, U7B13.IO_L2N_T0_13
- net FMC_A5: now also U13B13.IO_L3P_T0_DQS_13, U4FMC.FMC_A5/PF5, U5.A5, U6.A5; no longer IC1.A5, IC2.A5, U$1FMC.FMC_A5/PF5, U7B13.IO_L3P_T0_DQS_13
- net FMC_A6: now also U13B13.IO_L3N_T0_DQS_13, U4FMC.FMC_A6/PF12, U5.A6, U6.A6; no longer IC1.A6, IC2.A6, U$1FMC.FMC_A6/PF12, U7B13.IO_L3N_T0_DQS_13
- net FMC_A7: now also U13B13.IO_L4P_T0_13, U4FMC.FMC_A7/PF13, U5.A7, U6.A7; no longer IC1.A7, IC2.A7, U$1FMC.FMC_A7/PF13, U7B13.IO_L4P_T0_13
- net FMC_A8: now also U13B13.IO_L4N_T0_13, U4FMC.FMC_A8/PF14, U5.A8, U6.A8; no longer IC1.A8, IC2.A8, U$1FMC.FMC_A8/PF14, U7B13.IO_L4N_T0_13
- net FMC_A9: now also U13B13.IO_L5P_T0_13, U4FMC.FMC_A9/PF15, U5.A9, U6.A9; no longer IC1.A9, IC2.A9, U$1FMC.FMC_A9/PF15, U7B13.IO_L5P_T0_13
- net FMC_CLK: now also U13B13.IO_L12P_T1_MRCC_13, U4FMC.FMC_CLK/PD3; no longer U$1FMC.FMC_CLK/PD3, U7B13.IO_L12P_T1_MRCC_13
- net FMC_D0: now also U13B34.IO_0_34, U4FMC.PD14/FMC_D0, U5.DQ0, U6.DQ0; no longer IC1.DQ0, IC2.DQ0, U$1FMC.PD14/FMC_D0, U7B34.IO_0_34
- net FMC_D1: now also U13B34.IO_L1P_T0_34, U4FMC.PD15/FMC_D1, U5.DQ1, U6.DQ1; no longer IC1.DQ1, IC2.DQ1, U$1FMC.PD15/FMC_D1, U7B34.IO_L1P_T0_34
- net FMC_D10: now also U13B34.IO_L5N_T0_34, U4FMC.PE13/FMC_D10, U5.DQ10, U5.DQ9, U6.DQ10, U6.DQ9; no longer IC1.DQ10, IC1.DQ9, IC2.DQ10, IC2.DQ9, U$1FMC.PE13/FMC_D10, U7B34.IO_L5N_T0_34
- net FMC_D11: now also U13B34.IO_L6P_T0_34, U4FMC.PE14/FMC_D11, U5.DQ11, U6.DQ11; no longer IC1.DQ11, IC2.DQ11, U$1FMC.PE14/FMC_D11, U7B34.IO_L6P_T0_34
- net FMC_D12: now also U13B34.IO_L6N_T0_VREF_34, U4FMC.PE15/FMC_D12, U5.DQ12, U6.DQ12; no longer IC1.DQ12, IC2.DQ12, U$1FMC.PE15/FMC_D12, U7B34.IO_L6N_T0_VREF_34
- net FMC_D13: now also U13B34.IO_L7P_T1_34, U4FMC.PD8/FMC_D13, U5.DQ13, U6.DQ13; no longer IC1.DQ13, IC2.DQ13, U$1FMC.PD8/FMC_D13, U7B34.IO_L7P_T1_34
- net FMC_D14: now also U13B34.IO_L7N_T1_34, U4FMC.PD9/FMC_D14, U5.DQ14, U6.DQ14; no longer IC1.DQ14, IC2.DQ14, U$1FMC.PD9/FMC_D14, U7B34.IO_L7N_T1_34
- net FMC_D15: now also U13B34.IO_L8P_T1_34, U4FMC.PD10/FMC_D15, U5.DQ15, U6.DQ15; no longer IC1.DQ15, IC2.DQ15, U$1FMC.PD10/FMC_D15, U7B34.IO_L8P_T1_34
- net FMC_D16: now also U13B34.IO_L8N_T1_34, U4FMC.PH8/FMC_D16, U5.DQ16, U6.DQ16; no longer IC1.DQ16, IC2.DQ16, U$1FMC.PH8/FMC_D16, U7B34.IO_L8N_T1_34
- net FMC_D17: now also U13B34.IO_L9P_T1_DQS_34, U4FMC.PH9/FMC_D17, U5.DQ17, U6.DQ17; no longer IC1.DQ17, IC2.DQ17, U$1FMC.PH9/FMC_D17, U7B34.IO_L9P_T1_DQS_34
- net FMC_D18: now also U13B34.IO_L9N_T1_DQS_34, U4FMC.PH10/FMC_D18, U5.DQ18, U6.DQ18; no longer IC1.DQ18, IC2.DQ18, U$1FMC.PH10/FMC_D18, U7B34.IO_L9N_T1_DQS_34
- net FMC_D19: now also U13B34.IO_L10P_T1_34, U4FMC.PH11/FMC_D19, U5.DQ19, U6.DQ19; no longer IC1.DQ19, IC2.DQ19, U$1FMC.PH11/FMC_D19, U7B34.IO_L10P_T1_34
- net FMC_D2: now also U13B34.IO_L1N_T0_34, U4FMC.PD0/FMC_D2, U5.DQ2, U6.DQ2; no longer IC1.DQ2, IC2.DQ2, U$1FMC.PD0/FMC_D2, U7B34.IO_L1N_T0_34
- net FMC_D20: now also U13B34.IO_L10N_T1_34, U4FMC.PH12/FMC_D20, U5.DQ20, U6.DQ20; no longer IC1.DQ20, IC2.DQ20, U$1FMC.PH12/FMC_D20, U7B34.IO_L10N_T1_34
- net FMC_D21: now also U13B34.IO_L11P_T1_SRCC_34, U4FMC.PH13/FMC_D21, U5.DQ21, U6.DQ21; no longer IC1.DQ21, IC2.DQ21, U$1FMC.PH13/FMC_D21, U7B34.IO_L11P_T1_SRCC_34
- net FMC_D22: now also U13B34.IO_L11N_T1_SRCC_34, U4FMC.PH14/FMC_D22, U5.DQ22, U6.DQ22; no longer IC1.DQ22, IC2.DQ22, U$1FMC.PH14/FMC_D22, U7B34.IO_L11N_T1_SRCC_34
- net FMC_D23: now also U13B34.IO_L12P_T1_MRCC_34, U4FMC.PH15/FMC_D23, U5.DQ23, U6.DQ23; no longer IC1.DQ23, IC2.DQ23, U$1FMC.PH15/FMC_D23, U7B34.IO_L12P_T1_MRCC_34
- net FMC_D24: now also U13B34.IO_L12N_T1_MRCC_34, U4FMC.PI0/FMC_D24, U5.DQ24, U6.DQ24; no longer IC1.DQ24, IC2.DQ24, U$1FMC.PI0/FMC_D24, U7B34.IO_L12N_T1_MRCC_34
- net FMC_D25: now also U13B34.IO_L13P_T2_MRCC_34, U4FMC.PI1/FMC_D25, U5.DQ25, U6.DQ25; no longer IC1.DQ25, IC2.DQ25, U$1FMC.PI1/FMC_D25, U7B34.IO_L13P_T2_MRCC_34
- net FMC_D26: now also U13B34.IO_L13N_T2_MRCC_34, U4FMC.PI2/FMC_D26, U5.DQ26, U6.DQ26; no longer IC1.DQ26, IC2.DQ26, U$1FMC.PI2/FMC_D26, U7B34.IO_L13N_T2_MRCC_34
- net FMC_D27: now also U13B34.IO_L14P_T2_SRCC_34, U4FMC.PI3/FMC_D27, U5.DQ27, U6.DQ27; no longer IC1.DQ27, IC2.DQ27, U$1FMC.PI3/FMC_D27, U7B34.IO_L14P_T2_SRCC_34
- net FMC_D28: now also U13B34.IO_L14N_T2_SRCC_34, U4FMC.PI6/FMC_D28, U5.DQ28, U6.DQ28; no longer IC1.DQ28, IC2.DQ28, U$1FMC.PI6/FMC_D28, U7B34.IO_L14N_T2_SRCC_34
- net FMC_D29: now also U13B34.IO_L15P_T2_DQS_34, U4FMC.PI7/FMC_D29, U5.DQ29, U6.DQ29; no longer IC1.DQ29, IC2.DQ29, U$1FMC.PI7/FMC_D29, U7B34.IO_L15P_T2_DQS_34
- net FMC_D3: now also U13B34.IO_L2P_T0_34, U4FMC.PD1/FMC_D3, U5.DQ3, U6.DQ3; no longer IC1.DQ3, IC2.DQ3, U$1FMC.PD1/FMC_D3, U7B34.IO_L2P_T0_34
- net FMC_D30: now also U13B34.IO_L15N_T2_DQS_34, U4FMC.PI9/FMC_D30, U5.DQ30, U6.DQ30; no longer IC1.DQ30, IC2.DQ30, U$1FMC.PI9/FMC_D30, U7B34.IO_L15N_T2_DQS_34
- net FMC_D31: now also U13B34.IO_L16P_T2_34, U4FMC.PI10/FMC_D31, U5.DQ31, U6.DQ31; no longer IC1.DQ31, IC2.DQ31, U$1FMC.PI10/FMC_D31, U7B34.IO_L16P_T2_34
- net FMC_D4: now also U13B34.IO_L2N_T0_34, U4FMC.PE7/FMC_D4, U5.DQ4, U6.DQ4; no longer IC1.DQ4, IC2.DQ4, U$1FMC.PE7/FMC_D4, U7B34.IO_L2N_T0_34
- net FMC_D5: now also U13B34.IO_L3P_T0_DQS_34, U4FMC.PE8/FMC_D5, U5.DQ5, U6.DQ5; no longer IC1.DQ5, IC2.DQ5, U$1FMC.PE8/FMC_D5, U7B34.IO_L3P_T0_DQS_34
- net FMC_D6: now also U13B34.IO_L3N_T0_DQS_34, U4FMC.PE9/FMC_D6, U5.DQ6, U6.DQ6; no longer IC1.DQ6, IC2.DQ6, U$1FMC.PE9/FMC_D6, U7B34.IO_L3N_T0_DQS_34
- net FMC_D7: now also U13B34.IO_L4P_T0_34, U4FMC.PE10/FMC_D7, U5.DQ7, U6.DQ7; no longer IC1.DQ7, IC2.DQ7, U$1FMC.PE10/FMC_D7, U7B34.IO_L4P_T0_34
- net FMC_D8: now also U13B34.IO_L4N_T0_34, U4FMC.PE11/FMC_D8, U5.DQ8, U6.DQ8; no longer IC1.DQ8, IC2.DQ8, U$1FMC.PE11/FMC_D8, U7B34.IO_L4N_T0_34
- net FMC_D9: now also U13B34.IO_L5P_T0_34, U4FMC.PE12/FMC_D9; no longer U$1FMC.PE12/FMC_D9, U7B34.IO_L5P_T0_34
- net FMC_NBL0: now also U4FMC.FMC_NBL0/PE0, U5.DQM0, U6.DQM0; no longer IC1.DQM0, IC2.DQM0, U$1FMC.FMC_NBL0/PE0
- net FMC_NBL1: now also U4FMC.FMC_NBL1/PE1, U5.DQM1, U6.DQM1; no longer IC1.DQM1, IC2.DQM1, U$1FMC.FMC_NBL1/PE1
- net FMC_NBL2: now also U4FMC.FMC_NBL2/PI4, U5.DQM2, U6.DQM2; no longer IC1.DQM2, IC2.DQM2, U$1FMC.FMC_NBL2/PI4
- net FMC_NBL3: now also U4FMC.FMC_NBL3/PI5, U5.DQM3, U6.DQM3; no longer IC1.DQM3, IC2.DQM3, U$1FMC.FMC_NBL3/PI5
- net FMC_NE1: now also U13B34.IO_L16N_T2_34, U4FMC.FMC_NE1/PD7; no longer U$1FMC.FMC_NE1/PD7, U7B34.IO_L16N_T2_34
- net FMC_NL: now also U13B34.IO_L17P_T2_34, U4FMC.FMC_NL/PB7; no longer U$1FMC.FMC_NL/PB7, U7B34.IO_L17P_T2_34
- net FMC_NOE: now also U13B34.IO_L17N_T2_34, U4FMC.FMC_NOE/PD4; no longer U$1FMC.FMC_NOE/PD4, U7B34.IO_L17N_T2_34
- net FMC_NWAIT: now also U13B34.IO_L18P_T2_34, U4FMC.FMC_NWAIT/PD6; no longer U$1FMC.FMC_NWAIT/PD6, U7B34.IO_L18P_T2_34
- net FMC_NWE: now also U13B34.IO_L18N_T2_34, U4FMC.FMC_NWE/PD5; no longer U$1FMC.FMC_NWE/PD5, U7B34.IO_L18N_T2_34
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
